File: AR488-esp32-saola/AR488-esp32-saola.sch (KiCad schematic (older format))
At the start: 2 parts, among them J2 Conn_02x12_Odd_Even, U1 ESP32-S2-Saola-1

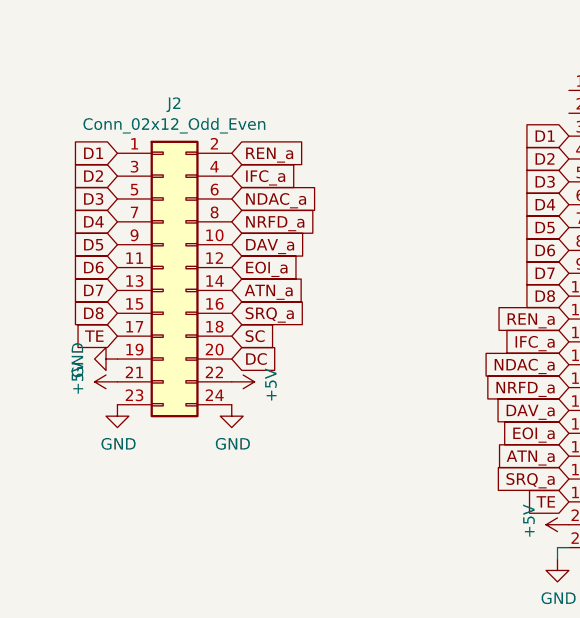
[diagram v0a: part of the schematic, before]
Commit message: Better pin assignment for the inter-PCB connector
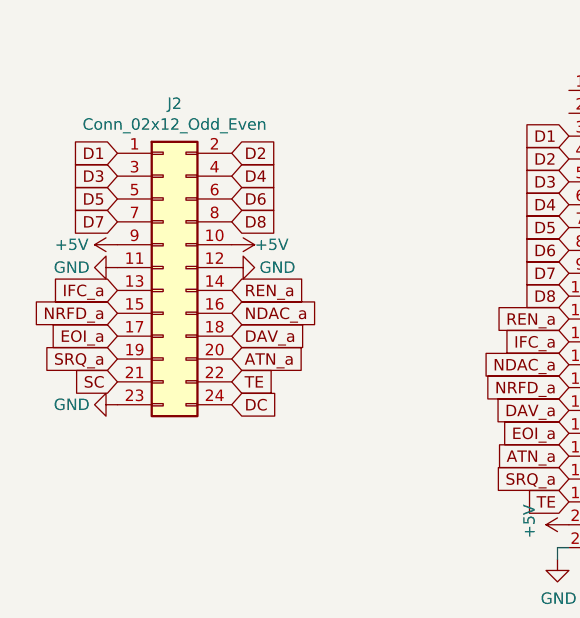
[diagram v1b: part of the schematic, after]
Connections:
- net +5V: now also J2.10 (Pin_10), J2.9 (Pin_9); no longer J2.21 (Pin_21), J2.22 (Pin_22)
- net ATN_a: now also J2.20 (Pin_20); no longer J2.14 (Pin_14)
- net D2: now also J2.2 (Pin_2); no longer J2.3 (Pin_3)
- net D3: now also J2.3 (Pin_3); no longer J2.5 (Pin_5)
- net D4: now also J2.4 (Pin_4); no longer J2.7 (Pin_7)
- net D5: now also J2.5 (Pin_5); no longer J2.9 (Pin_9)
- net D6: now also J2.6 (Pin_6); no longer J2.11 (Pin_11)
- net D7: now also J2.7 (Pin_7); no longer J2.13 (Pin_13)
- net D8: now also J2.8 (Pin_8); no longer J2.15 (Pin_15)
- net DAV_a: now also J2.18 (Pin_18); no longer J2.10 (Pin_10)
- net DC: now also J2.24 (Pin_24); no longer J2.20 (Pin_20)
- net EOI_a: now also J2.17 (Pin_17); no longer J2.12 (Pin_12)
- net GND: now also J2.11 (Pin_11), J2.12 (Pin_12); no longer J2.19 (Pin_19), J2.24 (Pin_24)
- net IFC_a: now also J2.13 (Pin_13); no longer J2.4 (Pin_4)
- net NDAC_a: now also J2.16 (Pin_16); no longer J2.6 (Pin_6)
- net NRFD_a: now also J2.15 (Pin_15); no longer J2.8 (Pin_8)
- net REN_a: now also J2.14 (Pin_14); no longer J2.2 (Pin_2)
- net SC: now also J2.21 (Pin_21); no longer J2.18 (Pin_18)
- net SRQ_a: now also J2.19 (Pin_19); no longer J2.16 (Pin_16)
- net TE: now also J2.22 (Pin_22); no longer J2.17 (Pin_17)
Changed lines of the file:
@@
 Text GLabel 3475 1675 0    50   Input ~ 0
 D1
+Text GLabel 3975 1675 2    50   Input ~ 0
+D2
 Text GLabel 3475 1775 0    50   Input ~ 0
-D2
+D3
+Text GLabel 3975 1775 2    50   Input ~ 0
+D4
 Text GLabel 3475 1875 0    50   Input ~ 0
-D3
+D5
+Text GLabel 3975 1875 2    50   Input ~ 0
+D6
 Text GLabel 3475 1975 0    50   Input ~ 0
-D4
-Text GLabel 3475 2075 0    50   Input ~ 0
-D5
-Text GLabel 3475 2175 0    50   Input ~ 0
-D6
+D7
+Text GLabel 3975 1975 2    50   Input ~ 0
+D8
+Text GLabel 3975 2275 2    50   Input ~ 0
+REN_a
 Text GLabel 3475 2275 0    50   Input ~ 0
-D7
+IFC_a
+Text GLabel 3975 2375 2    50   Input ~ 0
+NDAC_a
 Text GLabel 3475 2375 0    50   Input ~ 0
-D8
-Text GLabel 3975 1675 2    50   Input ~ 0
-REN_a
-Text GLabel 3975 1775 2    50   Input ~ 0
-IFC_a
-Text GLabel 3975 1875 2    50   Input ~ 0
-NDAC_a
-Text GLabel 3975 1975 2    50   Input ~ 0
 NRFD_a
-Text GLabel 3975 2075 2    50   Input ~ 0
+Text GLabel 3975 2475 2    50   Input ~ 0
 DAV_a
-Text GLabel 3975 2175 2    50   Input ~ 0
+Text GLabel 3475 2475 0    50   Input ~ 0
 EOI_a
-Text GLabel 3975 2275 2    50   Input ~ 0
+Text GLabel 3975 2575 2    50   Input ~ 0
 ATN_a
-Text GLabel 3975 2375 2    50   Input ~ 0
+Text GLabel 3475 2575 0    50   Input ~ 0
 SRQ_a
-Text GLabel 3475 2475 0    50   Input ~ 0
+Text GLabel 3975 2675 2    50   Input ~ 0
 TE
-Text GLabel 3975 2475 2    50   Input ~ 0
+Text GLabel 3475 2675 0    50   Input ~ 0
 SC
-Text GLabel 3975 2575 2    50   Input ~ 0
+Text GLabel 3975 2775 2    50   Input ~ 0
 DC
 $Comp
 L power:GND #PWR010
 U 1 1 6180B39E
-P 3975 2775
-F 0 "#PWR010" H 3975 2525 50  0001 C CNN
-F 1 "GND" H 3980 2602 50  0000 C CNN
-F 2 "" H 3975 2775 50  0001 C CNN
-F 3 "" H 3975 2775 50  0001 C CNN
-	1    3975 2775
-	1    0    0    -1
+P 3975 2175
+F 0 "#PWR010" H 3975 1925 50  0001 C CNN
+F 1 "GND" V 3975 1975 50  0000 C CNN
+F 2 "" H 3975 2175 50  0001 C CNN
+F 3 "" H 3975 2175 50  0001 C CNN
+	1    3975 2175
+	0    -1   -1   0
 $EndComp
 $Comp
 L power:GND #PWR03
 U 1 1 6180BA39
-P 3475 2775
-F 0 "#PWR03" H 3475 2525 50  0001 C CNN
-F 1 "GND" H 3480 2602 50  0000 C CNN
-F 2 "" H 3475 2775 50  0001 C CNN
-F 3 "" H 3475 2775 50  0001 C CNN
-	1    3475 2775
-	1    0    0    -1
+P 3475 2175
+F 0 "#PWR03" H 3475 1925 50  0001 C CNN
+F 1 "GND" V 3475 1975 50  0000 C CNN
+F 2 "" H 3475 2175 50  0001 C CNN
+F 3 "" H 3475 2175 50  0001 C CNN
+	1    3475 2175
+	0    1    1    0
 $EndComp
 $Comp
 L power:+5V #PWR09
 U 1 1 6180BF0B
-P 3975 2675
-F 0 "#PWR09" H 3975 2525 50  0001 C CNN
-F 1 "+5V" H 3990 2848 50  0000 C CNN
-F 2 "" H 3975 2675 50  0001 C CNN
-F 3 "" H 3975 2675 50  0001 C CNN
-	1    3975 2675
+P 3975 2075
+F 0 "#PWR09" H 3975 1925 50  0001 C CNN
+F 1 "+5V" V 3975 2250 50  0000 C CNN
+F 2 "" H 3975 2075 50  0001 C CNN
+F 3 "" H 3975 2075 50  0001 C CNN
+	1    3975 2075
 	0    1    1    0
 $EndComp
@@
 L power:+5V #PWR02
 U 1 1 6180CB7D
-P 3475 2675
-F 0 "#PWR02" H 3475 2525 50  0001 C CNN
-F 1 "+5V" H 3490 2848 50  0000 C CNN
-F 2 "" H 3475 2675 50  0001 C CNN
-F 3 "" H 3475 2675 50  0001 C CNN
-	1    3475 2675
+P 3475 2075
+F 0 "#PWR02" H 3475 1925 50  0001 C CNN
+F 1 "+5V" V 3475 2275 50  0000 C CNN
+F 2 "" H 3475 2075 50  0001 C CNN
+F 3 "" H 3475 2075 50  0001 C CNN
+	1    3475 2075
 	0    -1   -1   0
 $EndComp
@@
 L power:GND #PWR01
 U 1 1 6180D3A4
-P 3475 2575
-F 0 "#PWR01" H 3475 2325 50  0001 C CNN
-F 1 "GND" H 3480 2402 50  0000 C CNN
-F 2 "" H 3475 2575 50  0001 C CNN
-F 3 "" H 3475 2575 50  0001 C CNN
-	1    3475 2575
+P 3475 2775
+F 0 "#PWR01" H 3475 2525 50  0001 C CNN
+F 1 "GND" V 3475 2575 50  0000 C CNN
+F 2 "" H 3475 2775 50  0001 C CNN
+F 3 "" H 3475 2775 50  0001 C CNN
+	1    3475 2775
 	0    1    1    0
 $EndComp
